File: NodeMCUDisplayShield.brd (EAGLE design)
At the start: 34.3 x 6.7 mm, 2 parts

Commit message: Single-sided version
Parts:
- added X1: 332-02, con-garry:332-02
- moved ESP8266 6.96 mm to (15.2, 0.95), turned to 0 degrees
- moved TFT+TOUCH 5.08 mm to (17.8, 6.35), flipped to the top, turned to 0 degrees
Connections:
- net LED renamed D3
- net SCK renamed D5_SCK
- net SDI/MOSI renamed D7_SDI/MOSI
- net SODI/MISO renamed D6_SODI/MISO
- removed net CS: ESP8266.1, TFT+TOUCH.12
- removed net D/C: ESP8266.2, TFT+TOUCH.10
- removed net T_CS: ESP8266.4, TFT+TOUCH.4
- removed net T_IRQ: ESP8266.10, TFT+TOUCH.1
- new net D1: ESP8266.1, TFT+TOUCH.1
- new net D2: ESP8266.2, TFT+TOUCH.4
- new net D4: ESP8266.4, TFT+TOUCH.10
- new net D8: ESP8266.10, TFT+TOUCH.12
- net GND: now also X1.2
- net VCC: now also X1.1
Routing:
- net T_CS: track 17.1 -> 0.00 mm, vias 3 -> 0
- net D4: track 0.00 -> 14.9 mm
- net VCC: track 17.7 -> 28.5 mm, vias 1 -> 0
- net T_IRQ: track 9.46 -> 0.00 mm
- net D5_SCK: track 12.9 -> 21.1 mm
- net D6_SODI/MISO: track 15.1 -> 22.7 mm
- net D/C: track 6.92 -> 0.00 mm
- net D2: track 0.00 -> 6.45 mm
- net D1: track 0.00 -> 6.45 mm
- net D8: track 0.00 -> 6.45 mm
- net GND: track 14.5 -> 20.4 mm
- net D7_SDI/MOSI: track 18.9 -> 24.7 mm, vias 0 -> 1
- net CS: track 5.54 -> 0.00 mm
- net D3: track 12.0 -> 10.4 mm, vias 0 -> 1
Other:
- board size 34.3 x 6.7 mm -> 34.3 x 7.3 mm
- board text removed: "TOUCH"

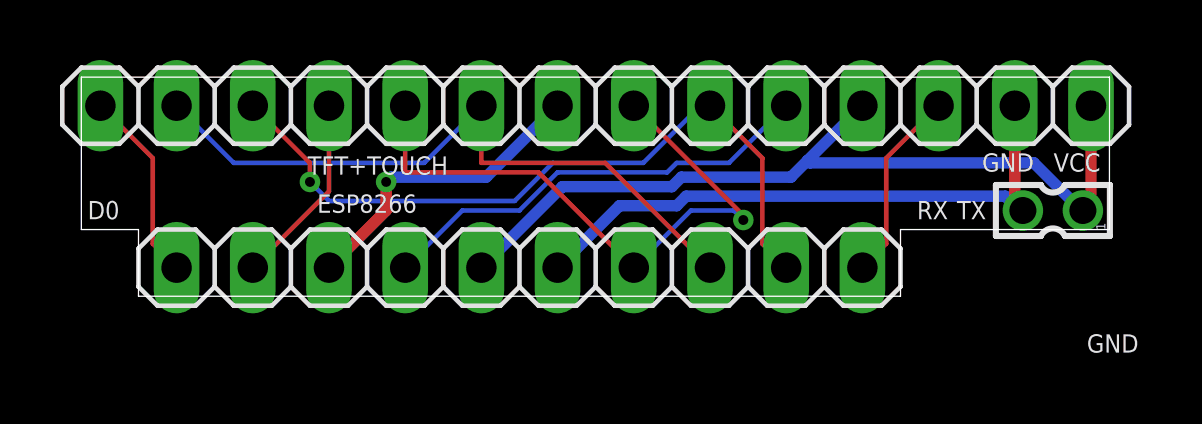
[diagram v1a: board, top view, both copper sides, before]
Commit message: https://pcbs.io/share/zd3qw SIngle-sided.
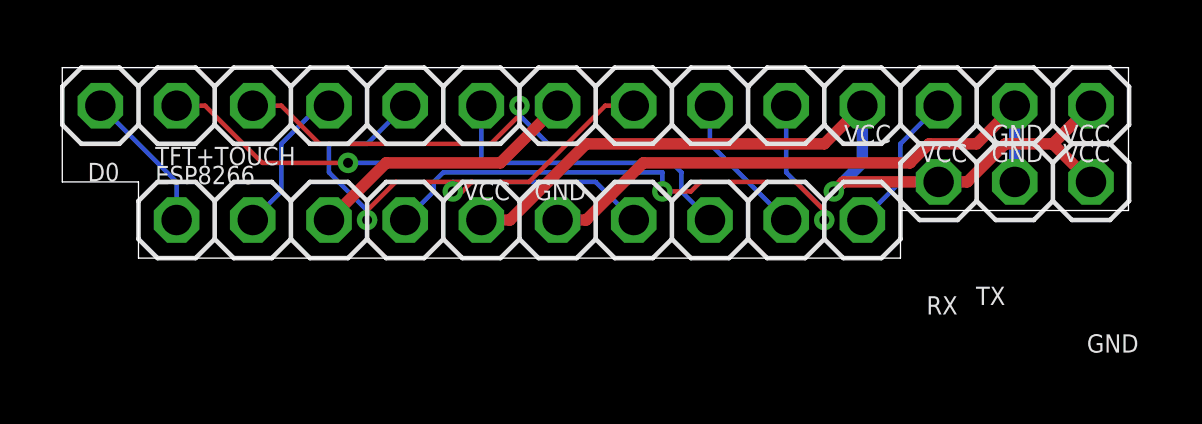
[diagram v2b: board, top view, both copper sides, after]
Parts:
- removed X1: 332-02, con-garry:332-02
- added JP1: (no value), pinhead_v2:1X03/OCT
- ESP8266: device pinhead:1X10 -> pinhead_v2:1X10/OCT
- TFT+TOUCH: device pinhead:1X14 -> pinhead_v2:1X14/OCT
- moved ESP8266 1.59 mm to (15.2, 2.54)
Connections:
- net GND: now also JP1.2; no longer X1.2
- net VCC: now also JP1.1, JP1.3; no longer X1.1
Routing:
- net D4: track 14.9 -> 20.6 mm, vias 0 -> 2
- net D5_SCK: track 21.1 -> 24.4 mm, vias 1 -> 2
- net D7_SDI/MOSI: track 24.7 -> 22.1 mm
- net D8: track 6.45 -> 4.86 mm
- net D1: track 6.45 -> 4.86 mm
- net D2: track 6.45 -> 5.05 mm
- net D3: track 10.4 -> 9.20 mm, vias 1 -> 0
- net D6_SODI/MISO: track 22.7 -> 21.6 mm, vias 0 -> 1
- net GND: track 20.4 -> 19.4 mm
- net VCC: track 28.5 -> 29.1 mm, vias 0 -> 1
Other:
- board size 34.3 x 7.3 mm -> 35.5 x 6.3 mm
